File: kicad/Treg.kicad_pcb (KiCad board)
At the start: 2 copper layers, 34 x 44 mm, 44 parts, among them J1 Conn_01x02, J2 Conn_01x02, J3 Conn_01x02, J4 Conn_01x02, J5 Conn_01x02, J7 Conn_01x07, J8 Conn_01x07, J9 Conn_01x02, U1 PMW3360, U2 TPS73601DBV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

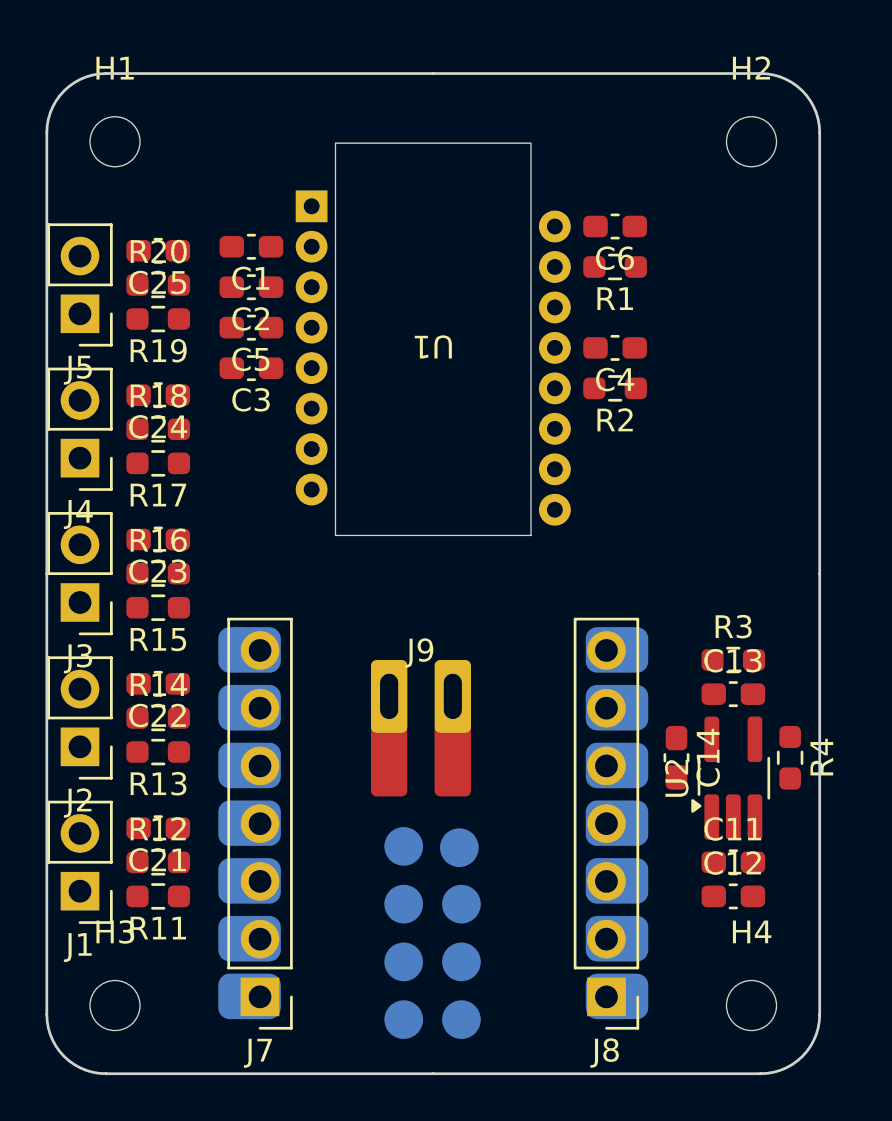
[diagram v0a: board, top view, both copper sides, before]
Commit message: replace parts with non-hand-solder, adjust refs
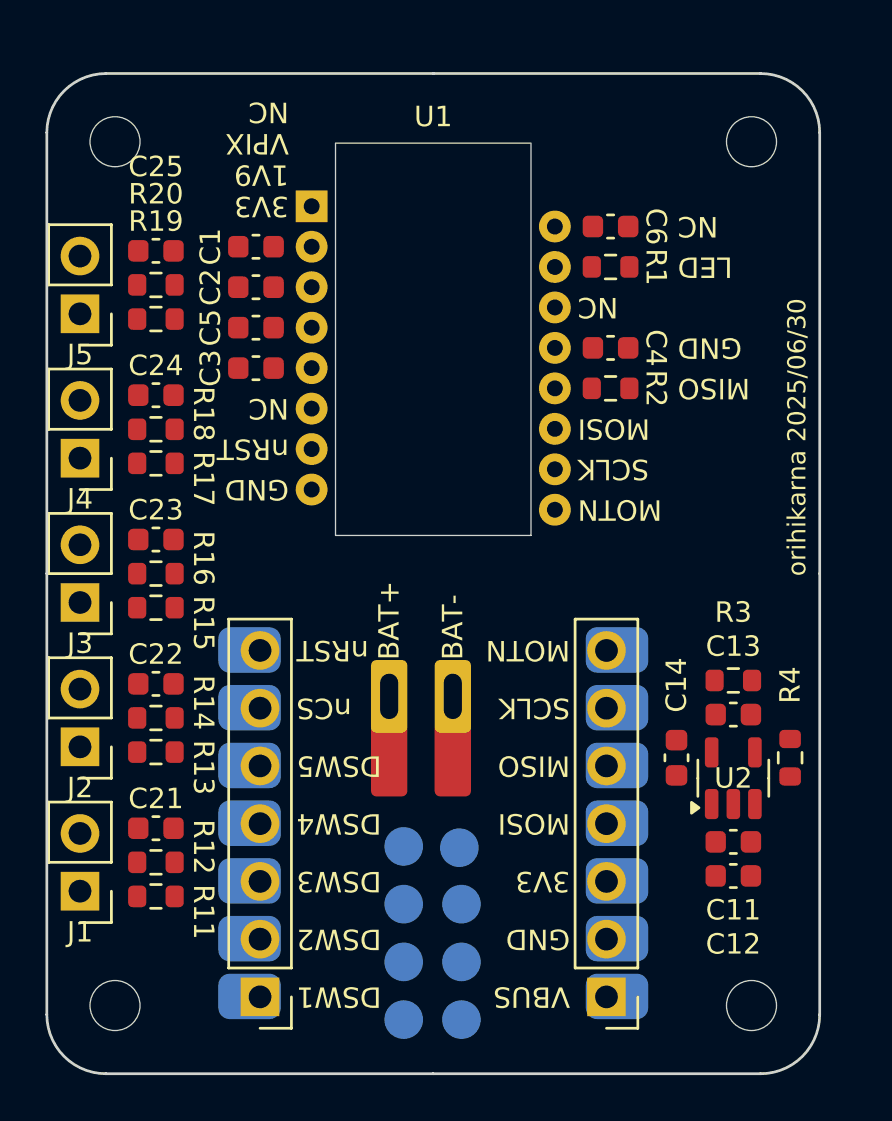
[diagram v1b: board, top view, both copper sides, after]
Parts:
- C1, C11, C12, C13, C14, C2, C21, C22, C23, C24, C25, C3, C4, C5, C6: footprint Capacitor_SMD:C_0603_1608Metric_Pad1.08x0.95mm_HandSolder -> Capacitor_SMD:C_0603_1608Metric
- R1, R11, R12, R13, R14, R15, R16, R17, R18, R19, R2, R20, R3, R4: footprint Resistor_SMD:R_0603_1608Metric_Pad0.98x0.95mm_HandSolder -> Resistor_SMD:R_0603_1608Metric
- U2: footprint Package_TO_SOT_SMD:TSOT-23-5_HandSoldering -> Package_TO_SOT_SMD:TSOT-23-5
- moved C11 0.90 mm to (113.2, 111.8)
- moved C12 0.90 mm to (113.2, 113.3)
- moved C13 0.90 mm to (113.2, 106.2)
- moved R3 0.90 mm to (113.2, 104.7)
- moved C1 0.20 mm to (92.2, 85.6)
- moved C2 0.20 mm to (92.2, 87.4)
- moved C3 0.20 mm to (92.2, 91.0)
- moved C4 0.20 mm to (107.8, 90.1)
- moved C5 0.20 mm to (92.2, 89.2)
- moved C6 0.20 mm to (107.8, 84.7)
- moved R1 0.20 mm to (107.8, 86.5)
- moved R2 0.20 mm to (107.8, 91.8)
- moved C21 0.10 mm to (87.8, 111.2)
- moved C22 0.10 mm to (87.8, 104.8)
- moved C23 0.10 mm to (87.8, 98.5)
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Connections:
- U1 pad 13: NCS -> GND
- U1 pad 4: VDD_1V9 -> 1V9
- U3 pad 6: NCS -> unconnected-(U3-GPIO23_D5_SCL-Pad6)
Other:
- copper layers 2 -> 4
- board text added: "1V9"
- board text added: "3V3"
- board text added: "BAT+"
- board text added: "BAT-"
- board text added: "DSW1"
- board text added: "DSW2"
- board text added: "DSW3"
- board text added: "DSW4"
- board text added: "DSW5"
- board text added: "GND"
- board text added: "LED"
- board text added: "MISO"
- board text added: "MOSI"
- board text added: "MOTN"
- board text added: "NC"
- board text added: "SCLK"
- board text added: "VBUS"
- board text added: "VPIX"
- board text added: "nCS"
- board text added: "nRST"
- board text added: "orihikarna 2025/06/30"
- board text removed: "orihikarna 25/06/30"

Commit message: wiring gnd
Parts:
- R1: footprint Resistor_SMD:R_0603_1608Metric -> Resistor_SMD:R_0603_1608Metric_Pad0.98x0.95mm_HandSolder
- moved C21 3.13 mm to (87.4, 114.3)
- moved R19 3.13 mm to (87.4, 85.7)
- moved C22 3.08 mm to (87.4, 107.9)
- moved R17 3.08 mm to (87.4, 92.1)
- moved C23 3.03 mm to (87.4, 101.5)
- moved R15 3.03 mm to (87.4, 98.5)
- moved C24 2.98 mm to (87.4, 95.1)
- moved R13 2.98 mm to (87.4, 104.9)
- moved C25 2.93 mm to (87.4, 88.7)
- moved R11 2.93 mm to (87.4, 111.3)
- moved J5 2.64 mm to (84.5, 85.9), turned to 0 degrees
- moved J4 2.59 mm to (84.5, 92.3), turned to 0 degrees
- moved J3 2.54 mm to (84.5, 98.7), turned to 0 degrees
- moved J2 2.49 mm to (84.5, 105.1), turned to 0 degrees
- moved J1 2.44 mm to (84.5, 111.5), turned to 0 degrees
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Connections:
- J7 pad 1: DSW1 -> unconnected-(J7-Pin_1-Pad1)
- J7 pad 2: DSW2 -> DSW1
- J7 pad 3: DSW3 -> DSW2
- J7 pad 4: DSW4 -> DSW3
- J7 pad 5: DSW5 -> DSW4
- J7 pad 6: NCS -> DSW5
- U3 pad 1: DSW1 -> unconnected-(U3-GPIO0_A0_D0-Pad1)
- U3 pad 2: DSW2 -> DSW1
- U3 pad 3: DSW3 -> DSW2
- U3 pad 4: DSW4 -> DSW3
- U3 pad 5: DSW5 -> DSW4
- U3 pad 6: unconnected-(U3-GPIO23_D5_SCL-Pad6) -> DSW5
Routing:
- net 3V3: track 0.00 -> 163.0 mm, vias 0 -> 6
- net GND: track 0.00 -> 110.2 mm, vias 0 -> 5
- net MISO: track 0.00 -> 27.4 mm
- net MOSI: track 0.00 -> 26.4 mm
- net DSW5: track 0.00 -> 20.2 mm
- net SCLK: track 0.00 -> 17.5 mm
- net DSW4: track 0.00 -> 16.5 mm
- net VBUS: track 0.00 -> 15.0 mm, vias 0 -> 2
- net DSW3: track 0.00 -> 12.6 mm
- net NRESET: track 0.00 -> 11.3 mm
- net DSW2: track 0.00 -> 8.85 mm
- net MOTION: track 0.00 -> 8.64 mm
- net VDD_1V9: track 0.00 -> 6.85 mm
- net DSW1: track 0.00 -> 5.97 mm
- net Net-(U2-FB): track 0.00 -> 5.01 mm
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
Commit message: wiring almost done
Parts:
- moved R4 2.85 mm to (113.0, 107.2), turned to 180 degrees
- moved C13 2.01 mm to (113.0, 104.2)
- moved C14 1.91 mm to (110.5, 110.0)
- moved C11 1.02 mm to (113.0, 112.8)
- moved C12 1.02 mm to (113.0, 114.3)
- moved R3 1.02 mm to (113.0, 105.7)
- moved U2 1.02 mm to (113.0, 110.0)
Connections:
- C13 pad 1: VDD_1V9 -> 1V9
- C14 pad 1: VDD_1V9 -> 1V9
- C5 pad 1: VDD_1V9 -> 1V9
- C6 pad 1: VDD_1V9 -> 1V9
- R1 pad 1: VDD_1V9 -> 1V9
- R3 pad 1: VDD_1V9 -> 1V9
- U2 pad 5: VDD_1V9 -> 1V9
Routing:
- net 1V9: track 1.88 -> 65.0 mm, vias 0 -> 1
- net VDD_1V9: track 6.85 -> 0.00 mm
- net VBUS: track 15.0 -> 19.6 mm
- net GND: track 110.2 -> 113.9 mm, vias 5 -> 4
- net MISO: track 27.4 -> 24.1 mm
- net MOSI: track 26.4 -> 23.0 mm
- net SCLK: track 17.5 -> 14.7 mm
- net MOTION: track 8.64 -> 7.28 mm
- net NRESET: track 11.3 -> 9.94 mm
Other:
- board text added: "nc"
- board text removed: "NC"

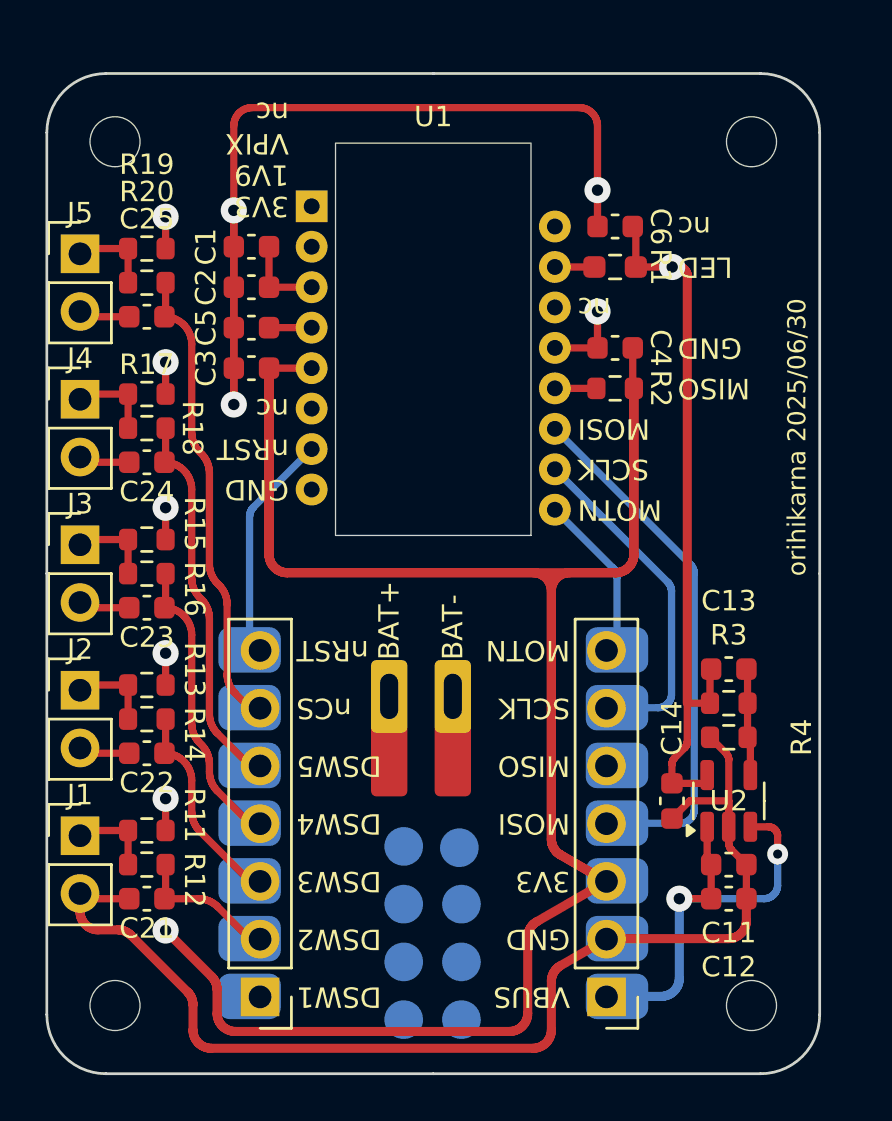
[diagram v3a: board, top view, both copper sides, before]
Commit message: add caps, jp
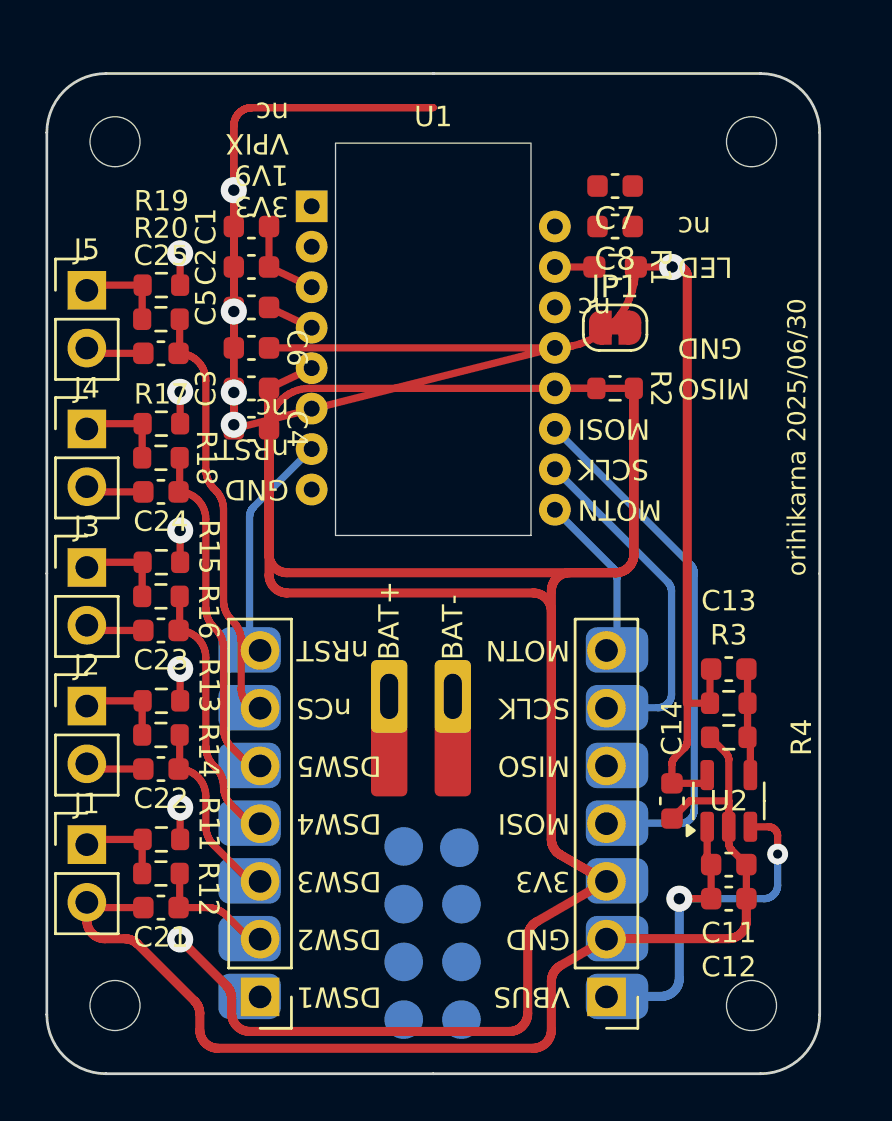
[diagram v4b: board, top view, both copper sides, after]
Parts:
- added C7: 100nF, Capacitor_SMD:C_0603_1608Metric, F.Cu at (108.0, 83.0)
- added C8: 10uF, Capacitor_SMD:C_0603_1608Metric, F.Cu at (108.0, 84.7)
- added JP1: SolderJumper_2_Bridged, Jumper:SolderJumper-2_P1.3mm_Bridged_RoundedPad1.0x1.5mm, F.Cu at (108.0, 89.2)
- C4, C6: value 100nF -> 10uF
- moved C6 16.9 mm to (92.0, 90.1)
- moved C4 16.4 mm to (92.0, 93.6)
- moved R19 1.73 mm to (88.0, 87.3)
- moved C25 1.72 mm to (88.0, 90.3)
- moved R20 1.72 mm to (88.0, 88.8)
- moved J5 1.64 mm to (84.8, 87.5)
- moved R17 1.45 mm to (88.0, 93.4)
- moved C24 1.44 mm to (88.0, 96.4)
- moved R18 1.44 mm to (88.0, 94.9)
- moved J4 1.34 mm to (84.8, 93.6)
- moved R15 1.19 mm to (88.0, 99.5)
- moved C23 1.18 mm to (88.0, 102.5)
- moved R16 1.18 mm to (88.0, 101.0)
- moved J3 1.04 mm to (84.8, 99.7)
- moved R13 0.95 mm to (88.0, 105.6)
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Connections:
- J7 pad 1: unconnected-(J7-Pin_1-Pad1) -> nc
- U1 pad 13: GND -> NCS
- U3 pad 1: unconnected-(U3-GPIO0_A0_D0-Pad1) -> nc
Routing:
- net 1V9: track 65.0 -> 81.5 mm
- net NCS: track 0.00 -> 14.6 mm
- net 3V3: track 163.0 -> 174.4 mm
- net GND: track 113.9 -> 121.6 mm
- net DSW5: track 20.2 -> 18.4 mm
- net DSW4: track 16.5 -> 14.9 mm
- net DSW3: track 12.6 -> 11.4 mm
- net DSW2: track 8.85 -> 7.90 mm
- net DSW1: track 5.97 -> 5.19 mm
